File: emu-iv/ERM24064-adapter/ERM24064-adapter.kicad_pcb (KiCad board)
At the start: 2 copper layers, 28.2 x 45.1 mm, 5 parts, among them J1 ERM24064-1-display, J2 ERM24064-1-mainboard, J3 Backlight_Connector_Mainboard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

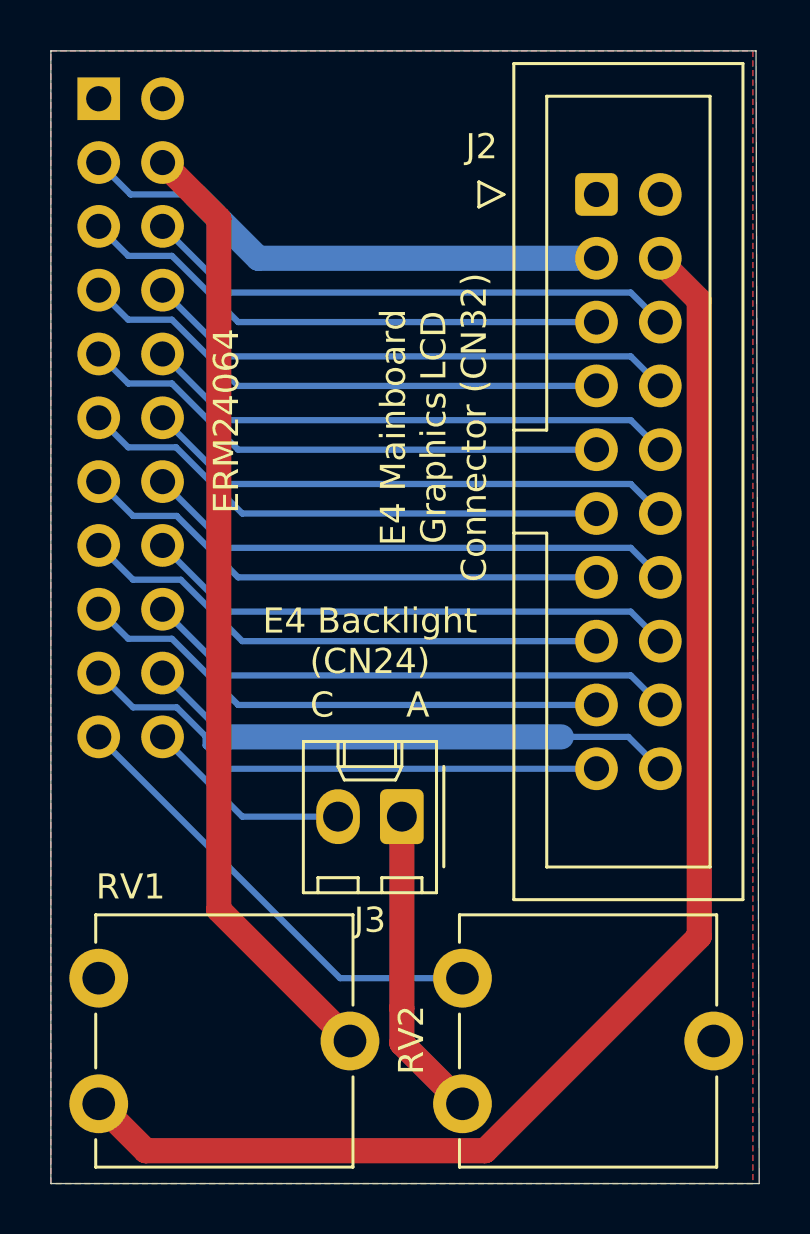
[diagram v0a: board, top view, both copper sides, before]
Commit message: correction wrt. to the current limiting resistor for the backlight led.
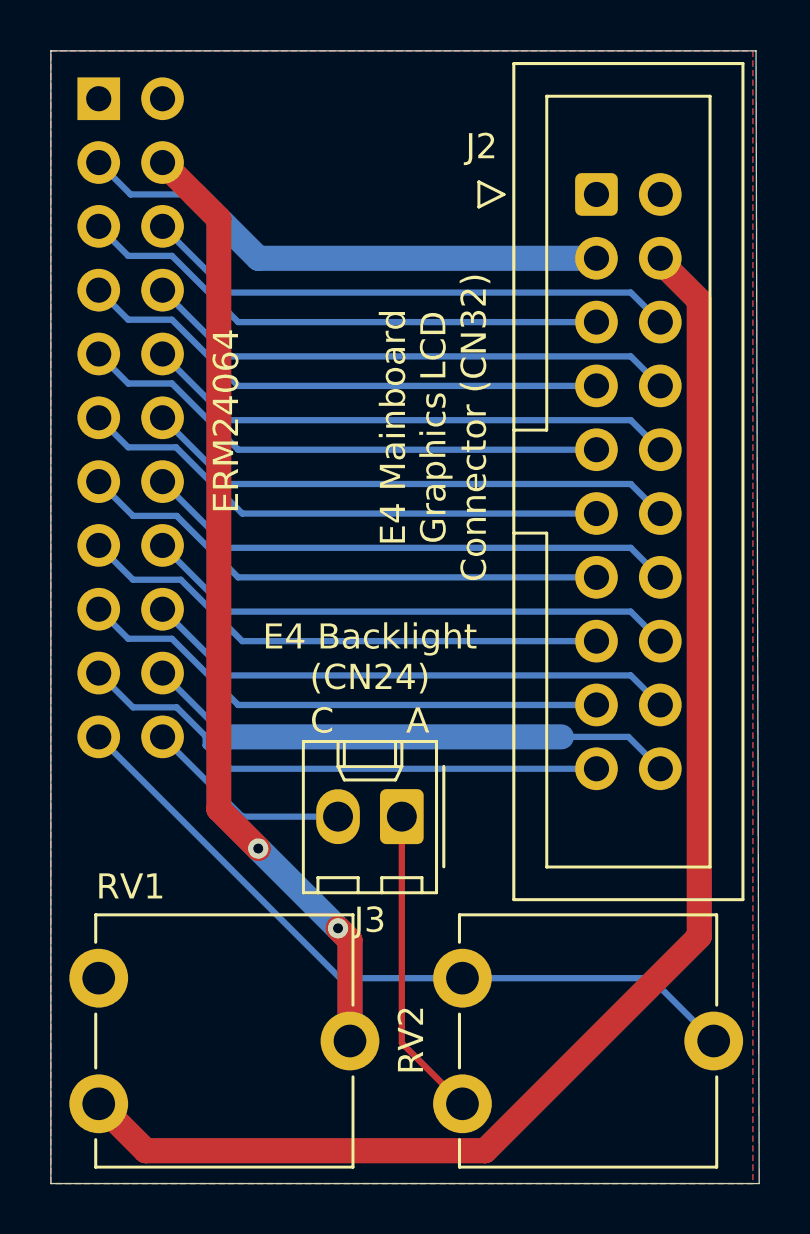
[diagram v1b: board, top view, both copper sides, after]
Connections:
- RV2 pad 2: Net-(RV2-Pad2) -> LED_A
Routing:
- net LED_A: track 18.5 -> 29.5 mm
- net Net-(J1-Pad4): vias 0 -> 2
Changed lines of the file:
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@@
     (thickness 1.6)
     (drawings 10)
-    (tracks 79)
+    (tracks 85)
     (zones 0)
     (modules 5)
-    (nets 25)
+    (nets 24)
   )
   (page A4)
@@
   (net 21 LED_A)
   (net 22 LED_K)
-  (net 23 "Net-(RV2-Pad2)")
-  (net 24 "Net-(J3-Pad1)")
+  (net 23 "Net-(J3-Pad1)")
   (net_class Default "This is the default net class."
     (clearance 0.2)
@@
     (add_net "Net-(J1-Pad4)")
     (add_net "Net-(J3-Pad1)")
-    (add_net "Net-(RV2-Pad2)")
     (add_net V0)
     (add_net VOUT)
@@
     )
     (pad 1 thru_hole circle (at 0 0) (size 2.34 2.34) (drill 1.3) (layers *.Cu *.Mask)
-      (net 24 "Net-(J3-Pad1)"))
+      (net 23 "Net-(J3-Pad1)"))
     (pad 2 thru_hole circle (at 10 -2.5) (size 2.34 2.34) (drill 1.3) (layers *.Cu *.Mask)
-      (net 23 "Net-(RV2-Pad2)"))
+      (net 21 LED_A))
     (pad 3 thru_hole circle (at 0 -5) (size 2.34 2.34) (drill 1.3) (layers *.Cu *.Mask)
       (net 21 LED_A))
@@
       (effects (font (size 1 1) (thickness 0.15)))
     )
-    (pad 1 thru_hole roundrect (at 0 0 180) (size 1.74 2.19) (drill 1.19) (layers *.Cu *.Mask) (roundrect_rratio 0.1436775862068966)
-      (net 24 "Net-(J3-Pad1)"))
+    (pad 1 thru_hole roundrect (at 0 0 180) (size 1.74 2.19) (drill 1.19) (layers *.Cu *.Mask) (roundrect_rratio 0.143678)
+      (net 23 "Net-(J3-Pad1)"))
     (pad 2 thru_hole oval (at 2.54 0 180) (size 1.74 2.19) (drill 1.19) (layers *.Cu *.Mask)
       (net 22 LED_K))
@@
     (effects (font (size 1 1) (thickness 0.15)) (justify mirror))
   )
-  (gr_text C (at 135.89 54.61) (layer F.SilkS)
+  (gr_text C (at 135.89 55.245) (layer F.SilkS)
     (effects (font (size 1 1) (thickness 0.15)))
   )
-  (gr_text A (at 139.7 54.61) (layer F.SilkS)
+  (gr_text A (at 139.7 55.245) (layer F.SilkS)
     (effects (font (size 1 1) (thickness 0.15)))
   )
@@
     (effects (font (size 1 1) (thickness 0.15)))
   )
-  (gr_text "E4 Backlight\n(CN24)" (at 137.795 52.07) (layer F.SilkS)
+  (gr_text "E4 Backlight\n(CN24)" (at 137.795 52.705) (layer F.SilkS)
     (effects (font (size 1 1) (thickness 0.15)))
   )
@@
   (segment (start 130.81 34.29) (end 128.27 34.29) (width 0.25) (layer B.Cu) (net 2))
   (segment (start 131.77999 35.25999) (end 129.54 33.02) (width 1) (layer F.Cu) (net 3))
-  (segment (start 131.77999 62.76499) (end 131.77999 35.25999) (width 1) (layer F.Cu) (net 3))
-  (segment (start 137 67.985) (end 131.77999 62.76499) (width 1) (layer F.Cu) (net 3))
+  (via (at 136.525 63.5) (size 0.8) (drill 0.4) (layers F.Cu B.Cu) (net 3))
+  (segment (start 137 63.975) (end 136.525 63.5) (width 1) (layer F.Cu) (net 3))
+  (segment (start 137 67.985) (end 137 63.975) (width 1) (layer F.Cu) (net 3))
+  (via (at 133.35 60.325) (size 0.8) (drill 0.4) (layers F.Cu B.Cu) (net 3))
+  (segment (start 136.525 63.5) (end 133.35 60.325) (width 1) (layer B.Cu) (net 3))
+  (segment (start 131.77999 58.75499) (end 131.77999 35.25999) (width 1) (layer F.Cu) (net 3))
+  (segment (start 133.35 60.325) (end 131.77999 58.75499) (width 1) (layer F.Cu) (net 3))
   (segment (start 128.175001 36.735001) (end 127 35.56) (width 0.25) (layer B.Cu) (net 4))
   (segment (start 129.914003 36.735001) (end 128.175001 36.735001) (width 0.25) (layer B.Cu) (net 4))
@@
   (segment (start 136.605 65.485) (end 127 55.88) (width 0.25) (layer B.Cu) (net 21))
   (segment (start 141.478 65.485) (end 136.605 65.485) (width 0.25) (layer B.Cu) (net 21))
+  (segment (start 148.978 65.485) (end 151.478 67.985) (width 0.25) (layer B.Cu) (net 21))
+  (segment (start 141.478 65.485) (end 148.978 65.485) (width 0.25) (layer B.Cu) (net 21))
   (segment (start 132.715 59.055) (end 136.525 59.055) (width 0.25) (layer B.Cu) (net 22))
   (segment (start 129.54 55.88) (end 132.715 59.055) (width 0.25) (layer B.Cu) (net 22))
-  (segment (start 139.065 68.072) (end 141.478 70.485) (width 1) (layer F.Cu) (net 24))
-  (segment (start 139.065 66.675) (end 139.065 59.055) (width 1) (layer F.Cu) (net 24))
-  (segment (start 139.065 68.072) (end 139.065 66.675) (width 1) (layer F.Cu) (net 24))
+  (segment (start 139.065 68.072) (end 141.478 70.485) (width 0.25) (layer F.Cu) (net 23))
+  (segment (start 139.065 59.055) (end 139.065 68.072) (width 0.25) (layer F.Cu) (net 23))
   (zone (net 1) (net_name GND) (layer F.Cu) (hatch edge 0.508)
     (connect_pads (clearance 0.508))
